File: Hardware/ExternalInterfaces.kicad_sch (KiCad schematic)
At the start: 6 parts, among them J3 USB_B_Micro, U2 CH340X

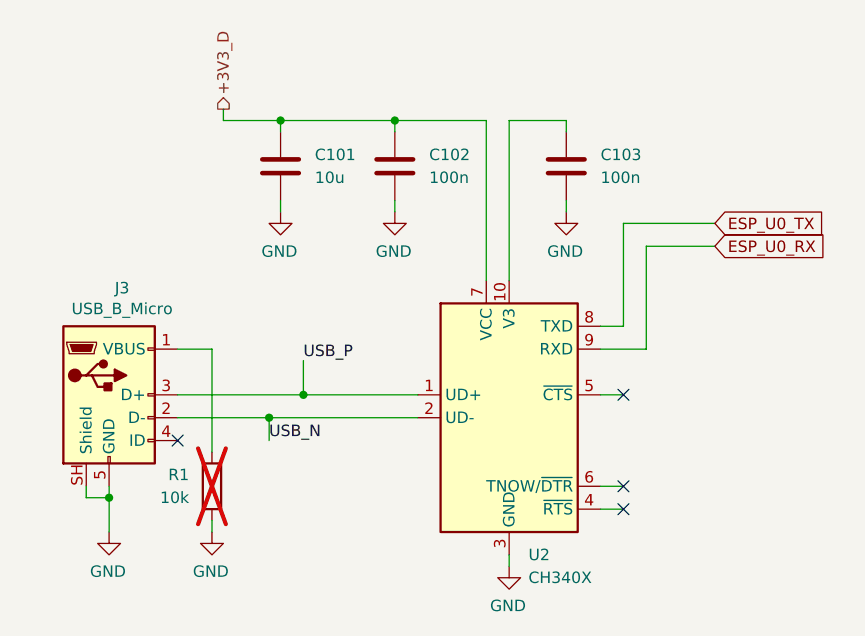
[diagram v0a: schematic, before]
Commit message: fix: #134
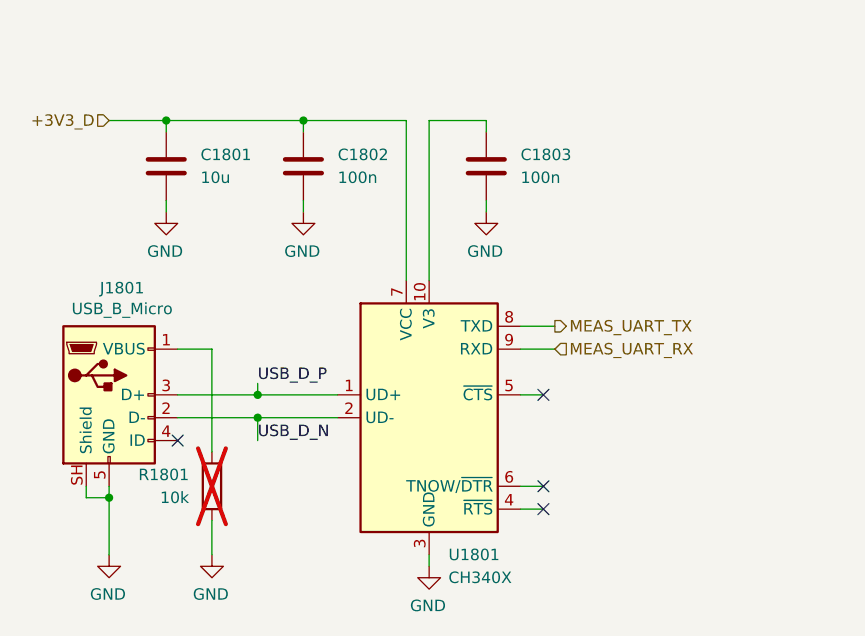
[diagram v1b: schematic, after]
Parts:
- removed C101: 10u, Capacitor_SMD:C_0805_2012Metric, symbol Device:C
- removed C102, C103: 100n, Capacitor_SMD:C_0805_2012Metric, symbol Device:C
- removed J3: USB_B_Micro, HardwareDataLogger:USB_Micro-B_Molex-105017-0001_Extra_Mechanical_Pads, symbol Connector:USB_B_Micro
- removed R1: 10k, Resistor_SMD:R_0805_2012Metric, symbol Device:R
- removed U2: CH340X, Package_SO:MSOP-10_3x3mm_P0.5mm, symbol Interface_USB:CH340X
- added C1801: 10u, Capacitor_SMD:C_0805_2012Metric, symbol Device:C
- added C1802, C1803: 100n, Capacitor_SMD:C_0805_2012Metric, symbol Device:C
- added J1801: USB_B_Micro, HardwareDataLogger:USB_Micro-B_Molex-105017-0001_Extra_Mechanical_Pads, symbol Connector:USB_B_Micro
- added R1801: 10k, Resistor_SMD:R_0805_2012Metric, symbol Device:R
- added U1801: CH340X, Package_SO:MSOP-10_3x3mm_P0.5mm, symbol Interface_USB:CH340X
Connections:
- net +3V3_D: now also C1801.1, C1802.1, U1801.7 (VCC)
- net GND: now also C1801.2, C1802.2, C1803.2, J1801.5 (GND), J1801.SH (Shield), R1801.1, U1801.3 (GND)
- new net: J1801.1 (VBUS), R1801.2
- new net: C1803.1, U1801.10 (V3)
- new net MEAS_UART_RX: U1801.9 (RXD)
- new net MEAS_UART_TX: U1801.8 (TXD)
- new net USB_D_N: J1801.2 (D-), U1801.2 (UD-)
- new net USB_D_P: J1801.3 (D+), U1801.1 (UD+)
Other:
- title: User Interface -> External Interfaces

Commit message: fix: #170, fix #144
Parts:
- J1801: footprint HardwareDataLogger:USB_Micro-B_Molex-105017-0001_Extra_Mechanical_Pads -> GammaSpectrometer:USB_Micro-B_Molex-105017-0001_Extra_Mechanical_Pads
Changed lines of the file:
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@@
 		(in_pos_files yes)
 		(dnp no)
-		(property "Reference" "#PWR01804"
+		(property "Reference" "#PWR1804"
 			(at 82.55 59.69 0)
 			(hide yes)
@@
 			(project "GammaSpectrometer"
 				(path "/d6192878-4721-4ef4-99ff-dbbad0502886/42540219-26d7-4d17-b5bd-2b115da83203"
-					(reference "#PWR01804")
+					(reference "#PWR1804")
 					(unit 1)
 				)
@@
 		(in_pos_files yes)
 		(dnp no)
-		(property "Reference" "#PWR01803"
+		(property "Reference" "#PWR1803"
 			(at 72.39 97.79 0)
 			(hide yes)
@@
 			(project "GammaSpectrometer"
 				(path "/d6192878-4721-4ef4-99ff-dbbad0502886/42540219-26d7-4d17-b5bd-2b115da83203"
-					(reference "#PWR01803")
+					(reference "#PWR1803")
 					(unit 1)
 				)
@@
 		(in_pos_files yes)
 		(dnp no)
-		(property "Reference" "#PWR01801"
+		(property "Reference" "#PWR1801"
 			(at 60.96 97.79 0)
 			(hide yes)
@@
 			(project "GammaSpectrometer"
 				(path "/d6192878-4721-4ef4-99ff-dbbad0502886/42540219-26d7-4d17-b5bd-2b115da83203"
-					(reference "#PWR01801")
+					(reference "#PWR1801")
 					(unit 1)
 				)
@@
 		(in_pos_files yes)
 		(dnp no)
-		(property "Reference" "#PWR01802"
+		(property "Reference" "#PWR1802"
 			(at 67.31 59.69 0)
 			(hide yes)
@@
 			(project "GammaSpectrometer"
 				(path "/d6192878-4721-4ef4-99ff-dbbad0502886/42540219-26d7-4d17-b5bd-2b115da83203"
-					(reference "#PWR01802")
+					(reference "#PWR1802")
 					(unit 1)
 				)
@@
 			)
 		)
-		(property "Footprint" "HardwareDataLogger:USB_Micro-B_Molex-105017-0001_Extra_Mechanical_Pads"
+		(property "Footprint" "GammaSpectrometer:USB_Micro-B_Molex-105017-0001_Extra_Mechanical_Pads"
 			(at 64.77 74.93 0)
 			(hide yes)
@@
 		(in_pos_files yes)
 		(dnp no)
-		(property "Reference" "#PWR01805"
+		(property "Reference" "#PWR1805"
 			(at 96.52 99.06 0)
 			(hide yes)
@@
 			(project "GammaSpectrometer"
 				(path "/d6192878-4721-4ef4-99ff-dbbad0502886/42540219-26d7-4d17-b5bd-2b115da83203"
-					(reference "#PWR01805")
+					(reference "#PWR1805")
 					(unit 1)
 				)
@@
 		(in_pos_files yes)
 		(dnp no)
-		(property "Reference" "#PWR01806"
+		(property "Reference" "#PWR1806"
 			(at 102.87 59.69 0)
 			(hide yes)
@@
 			(project "GammaSpectrometer"
 				(path "/d6192878-4721-4ef4-99ff-dbbad0502886/42540219-26d7-4d17-b5bd-2b115da83203"
-					(reference "#PWR01806")
-					(unit 1)
-				)
+					(reference "#PWR1806")
+					(unit 1)
+				)
